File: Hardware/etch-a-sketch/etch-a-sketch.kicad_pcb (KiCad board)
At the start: 2 copper layers, 100 x 42 mm, 37 parts, among them J1 USART, J2 Conn_02x05_Odd_Even, J3 OLED, J4 Power Connector, SW1 Encoder 1, SW2 Encoder 2, U1 AMS1117-3.3, U2 STM32F401RET6

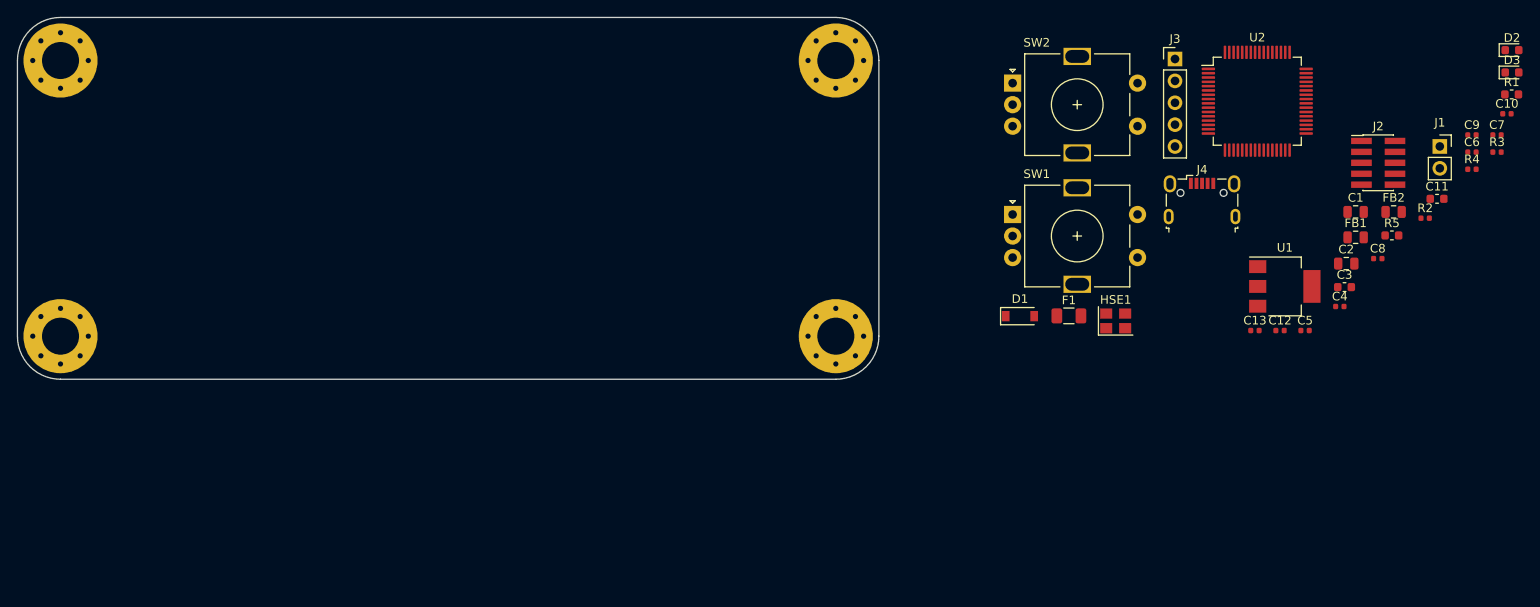
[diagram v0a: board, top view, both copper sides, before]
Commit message: fix: resize PCB outline to be 62mm tall
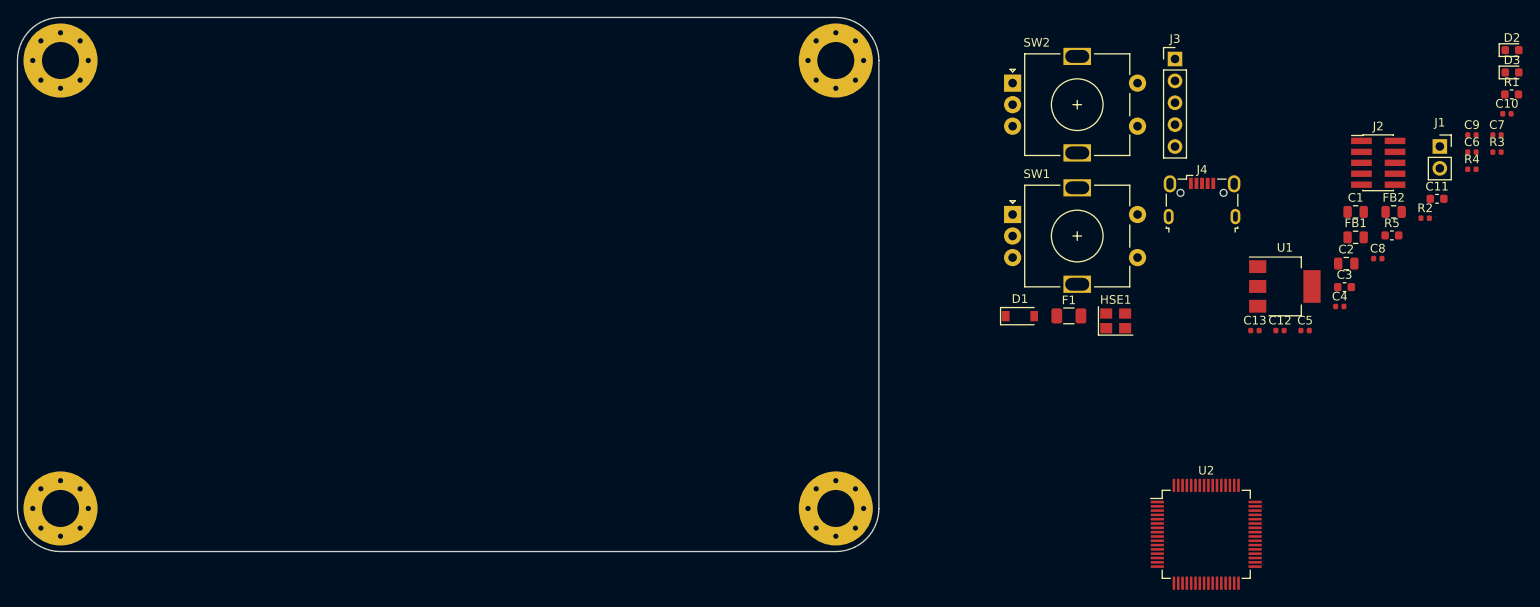
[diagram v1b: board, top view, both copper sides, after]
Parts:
- moved U2 50.6 mm to (158.0, 80.0)
- moved H3 20.0 mm to (25.0, 77.0)
- moved H4 20.0 mm to (115.0, 77.0)
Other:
- board size 100 x 42 mm -> 100 x 62 mm
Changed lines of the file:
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@@
   )
   (module MountingHole:MountingHole_4.3mm_M4_Pad_Via (layer F.Cu)
-    (at 25 57)
+    (at 25 77)
     (descr "Mounting Hole 4.3mm, M4")
     (tags "mounting hole 4.3mm m4")
@@
   )
   (module MountingHole:MountingHole_4.3mm_M4_Pad_Via (layer F.Cu)
-    (at 115 57)
+    (at 115 77)
     (descr "Mounting Hole 4.3mm, M4")
     (tags "mounting hole 4.3mm m4")
@@
   )
   (module Package_QFP:LQFP-64_10x10mm_P0.5mm (layer F.Cu)
-    (at 163.925001 29.725001)
+    (at 158 80)
     (descr "LQFP, 64 Pin (https://www.analog.com/media/en/technical-documentation/data-sheets/ad7606_7606-6_7606-4.pdf), generated with kicad-footprint-generator ipc_gullwing_generator.py")
     (tags "LQFP QFP")
@@
     )
   )
-  (gr_arc (start 115 57) (end 115 62) (angle -90) (layer Edge.Cuts) (width 0.05))
+  (gr_arc (start 115 77) (end 115 82) (angle -90) (layer Edge.Cuts) (width 0.05))
   (gr_arc (start 115 25) (end 120 25) (angle -90) (layer Edge.Cuts) (width 0.05))
-  (gr_arc (start 25 57) (end 20 57) (angle -90) (layer Edge.Cuts) (width 0.05))
+  (gr_arc (start 25 77) (end 20 77) (angle -90) (layer Edge.Cuts) (width 0.05))
   (gr_line (start 25 20) (end 115 20) (layer Edge.Cuts) (width 0.05))
   (gr_arc (start 25 25) (end 25 20) (angle -90) (layer Edge.Cuts) (width 0.05))
-  (gr_line (start 20 57) (end 20 25) (layer Edge.Cuts) (width 0.05))
-  (gr_line (start 115 62) (end 25 62) (layer Edge.Cuts) (width 0.05))
-  (gr_line (start 120 25) (end 120 57) (layer Edge.Cuts) (width 0.05))
+  (gr_line (start 20 77) (end 20 25) (layer Edge.Cuts) (width 0.05))
+  (gr_line (start 115 82) (end 25 82) (layer Edge.Cuts) (width 0.05))
+  (gr_line (start 120 25) (end 120 77) (layer Edge.Cuts) (width 0.05))
 )

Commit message: feat: move MCU to centre of board
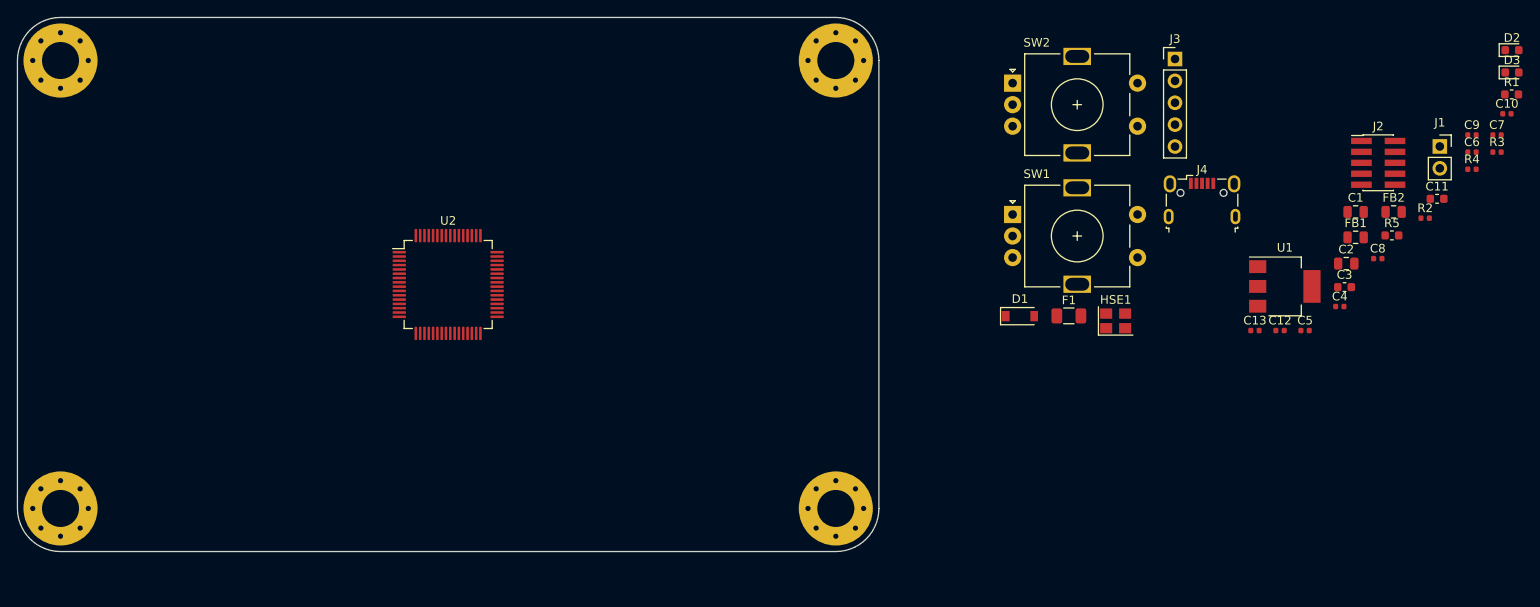
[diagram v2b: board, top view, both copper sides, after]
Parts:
- moved U2 92.7 mm to (70.0, 51.0)
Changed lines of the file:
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@@
   )
   (module Package_QFP:LQFP-64_10x10mm_P0.5mm (layer F.Cu)
-    (at 158 80)
+    (at 70 51)
     (descr "LQFP, 64 Pin (https://www.analog.com/media/en/technical-documentation/data-sheets/ad7606_7606-6_7606-4.pdf), generated with kicad-footprint-generator ipc_gullwing_generator.py")
     (tags "LQFP QFP")

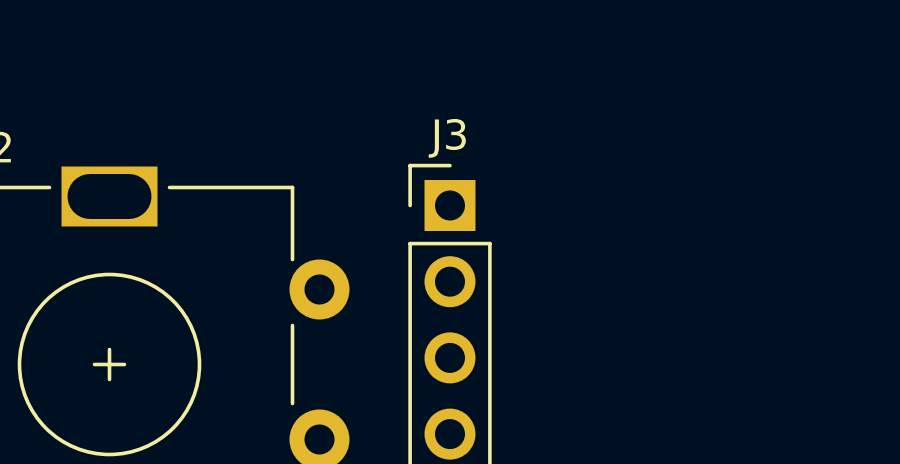
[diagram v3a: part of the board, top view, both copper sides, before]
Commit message: fix: actually maybe better to keep the OLED socketed
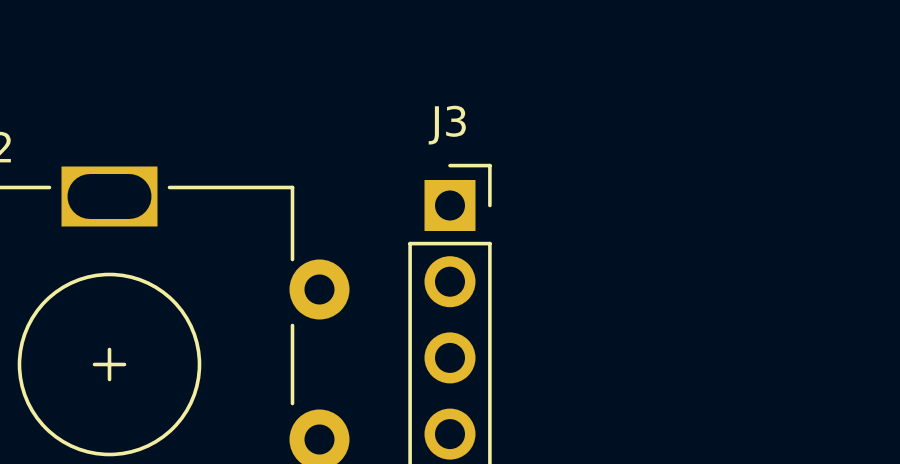
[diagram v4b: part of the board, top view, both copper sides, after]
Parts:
- J3: footprint Connector_PinHeader_2.54mm:PinHeader_1x05_P2.54mm_Vertical -> Connector_PinSocket_2.54mm:PinSocket_1x05_P2.54mm_Vertical
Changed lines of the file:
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@@
     (add_net VCC)
+  )
+  (module Connector_PinSocket_2.54mm:PinSocket_1x05_P2.54mm_Vertical (layer F.Cu)
+    (at 154.375001 24.825001)
+    (descr "Through hole straight socket strip, 1x05, 2.54mm pitch, single row (from Kicad 4.0.7), script generated")
+    (tags "Through hole socket strip THT 1x05 2.54mm single row")
+    (fp_text reference J3 (at 0 -2.77) (layer F.SilkS)
+      (effects (font (size 1 1) (thickness 0.15)))
+    )
+    (fp_text value OLED (at 0 12.93) (layer F.Fab)
+      (effects (font (size 1 1) (thickness 0.15)))
+    )
+    (fp_text user %R (at 0 5.08 90) (layer F.Fab)
+      (effects (font (size 1 1) (thickness 0.15)))
+    )
+    (fp_line (start -1.8 11.9) (end -1.8 -1.8) (layer F.CrtYd) (width 0.05))
+    (fp_line (start 1.75 11.9) (end -1.8 11.9) (layer F.CrtYd) (width 0.05))
+    (fp_line (start 1.75 -1.8) (end 1.75 11.9) (layer F.CrtYd) (width 0.05))
+    (fp_line (start -1.8 -1.8) (end 1.75 -1.8) (layer F.CrtYd) (width 0.05))
+    (fp_line (start 0 -1.33) (end 1.33 -1.33) (layer F.SilkS) (width 0.12))
+    (fp_line (start 1.33 -1.33) (end 1.33 0) (layer F.SilkS) (width 0.12))
+    (fp_line (start 1.33 1.27) (end 1.33 11.49) (layer F.SilkS) (width 0.12))
+    (fp_line (start -1.33 11.49) (end 1.33 11.49) (layer F.SilkS) (width 0.12))
+    (fp_line (start -1.33 1.27) (end -1.33 11.49) (layer F.SilkS) (width 0.12))
+    (fp_line (start -1.33 1.27) (end 1.33 1.27) (layer F.SilkS) (width 0.12))
+    (fp_line (start -1.27 11.43) (end -1.27 -1.27) (layer F.Fab) (width 0.1))
+    (fp_line (start 1.27 11.43) (end -1.27 11.43) (layer F.Fab) (width 0.1))
+    (fp_line (start 1.27 -0.635) (end 1.27 11.43) (layer F.Fab) (width 0.1))
+    (fp_line (start 0.635 -1.27) (end 1.27 -0.635) (layer F.Fab) (width 0.1))
+    (fp_line (start -1.27 -1.27) (end 0.635 -1.27) (layer F.Fab) (width 0.1))
+    (pad 5 thru_hole oval (at 0 10.16) (size 1.7 1.7) (drill 1) (layers *.Cu *.Mask)
+      (net 1 GND))
+    (pad 4 thru_hole oval (at 0 7.62) (size 1.7 1.7) (drill 1) (layers *.Cu *.Mask)
+      (net 24 "Net-(J3-Pad4)"))
+    (pad 3 thru_hole oval (at 0 5.08) (size 1.7 1.7) (drill 1) (layers *.Cu *.Mask)
+      (net 23 OLED_SCL))
+    (pad 2 thru_hole oval (at 0 2.54) (size 1.7 1.7) (drill 1) (layers *.Cu *.Mask)
+      (net 22 OLED_SDA))
+    (pad 1 thru_hole rect (at 0 0) (size 1.7 1.7) (drill 1) (layers *.Cu *.Mask)
+      (net 3 +3V3))
+    (model ${KISYS3DMOD}/Connector_PinSocket_2.54mm.3dshapes/PinSocket_1x05_P2.54mm_Vertical.wrl
+      (at (xyz 0 0 0))
+      (scale (xyz 1 1 1))
+      (rotate (xyz 0 0 0))
+    )
   )
   (module Capacitor_SMD:C_0805_2012Metric (layer F.Cu)
@@
       (at (xyz 0 0 0))
       (scale (xyz 1 1 1))
-      (rotate (xyz 0 0 0))
-    )
-  )
-  (module Connector_PinHeader_2.54mm:PinHeader_1x05_P2.54mm_Vertical (layer F.Cu)
-    (at 154.375001 24.825001)
-    (descr "Through hole straight pin header, 1x05, 2.54mm pitch, single row")
-    (tags "Through hole pin header THT 1x05 2.54mm single row")
-    (fp_text reference J3 (at 0 -2.33) (layer F.SilkS)
-      (effects (font (size 1 1) (thickness 0.15)))
-    )
-    (fp_text value OLED (at 0 12.49) (layer F.Fab)
-      (effects (font (size 1 1) (thickness 0.15)))
-    )
-    (fp_line (start -0.635 -1.27) (end 1.27 -1.27) (layer F.Fab) (width 0.1))
-    (fp_line (start 1.27 -1.27) (end 1.27 11.43) (layer F.Fab) (width 0.1))
-    (fp_line (start 1.27 11.43) (end -1.27 11.43) (layer F.Fab) (width 0.1))
-    (fp_line (start -1.27 11.43) (end -1.27 -0.635) (layer F.Fab) (width 0.1))
-    (fp_line (start -1.27 -0.635) (end -0.635 -1.27) (layer F.Fab) (width 0.1))
-    (fp_line (start -1.33 11.49) (end 1.33 11.49) (layer F.SilkS) (width 0.12))
-    (fp_line (start -1.33 1.27) (end -1.33 11.49) (layer F.SilkS) (width 0.12))
-    (fp_line (start 1.33 1.27) (end 1.33 11.49) (layer F.SilkS) (width 0.12))
-    (fp_line (start -1.33 1.27) (end 1.33 1.27) (layer F.SilkS) (width 0.12))
-    (fp_line (start -1.33 0) (end -1.33 -1.33) (layer F.SilkS) (width 0.12))
-    (fp_line (start -1.33 -1.33) (end 0 -1.33) (layer F.SilkS) (width 0.12))
-    (fp_line (start -1.8 -1.8) (end -1.8 11.95) (layer F.CrtYd) (width 0.05))
-    (fp_line (start -1.8 11.95) (end 1.8 11.95) (layer F.CrtYd) (width 0.05))
-    (fp_line (start 1.8 11.95) (end 1.8 -1.8) (layer F.CrtYd) (width 0.05))
-    (fp_line (start 1.8 -1.8) (end -1.8 -1.8) (layer F.CrtYd) (width 0.05))
-    (fp_text user %R (at 0 5.08 90) (layer F.Fab)
-      (effects (font (size 1 1) (thickness 0.15)))
-    )
-    (pad 1 thru_hole rect (at 0 0) (size 1.7 1.7) (drill 1) (layers *.Cu *.Mask)
-      (net 3 +3V3))
-    (pad 2 thru_hole oval (at 0 2.54) (size 1.7 1.7) (drill 1) (layers *.Cu *.Mask)
-      (net 22 OLED_SDA))
-    (pad 3 thru_hole oval (at 0 5.08) (size 1.7 1.7) (drill 1) (layers *.Cu *.Mask)
-      (net 23 OLED_SCL))
-    (pad 4 thru_hole oval (at 0 7.62) (size 1.7 1.7) (drill 1) (layers *.Cu *.Mask)
-      (net 24 "Net-(J3-Pad4)"))
-    (pad 5 thru_hole oval (at 0 10.16) (size 1.7 1.7) (drill 1) (layers *.Cu *.Mask)
-      (net 1 GND))
-    (model ${KISYS3DMOD}/Connector_PinHeader_2.54mm.3dshapes/PinHeader_1x05_P2.54mm_Vertical.wrl
-      (at (xyz 0 0 0))
-      (scale (xyz 1 1 1))

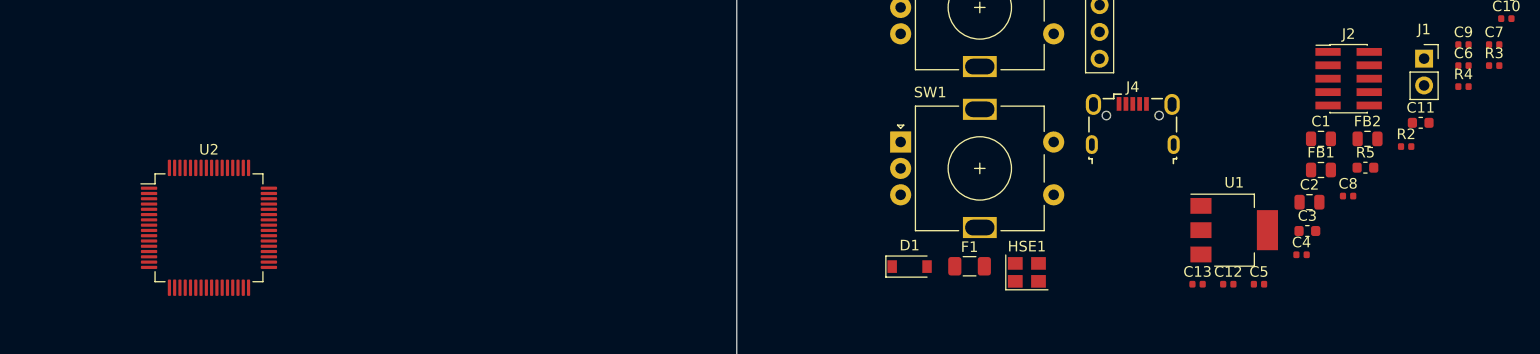
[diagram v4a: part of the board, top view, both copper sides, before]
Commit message: feat: place HSE
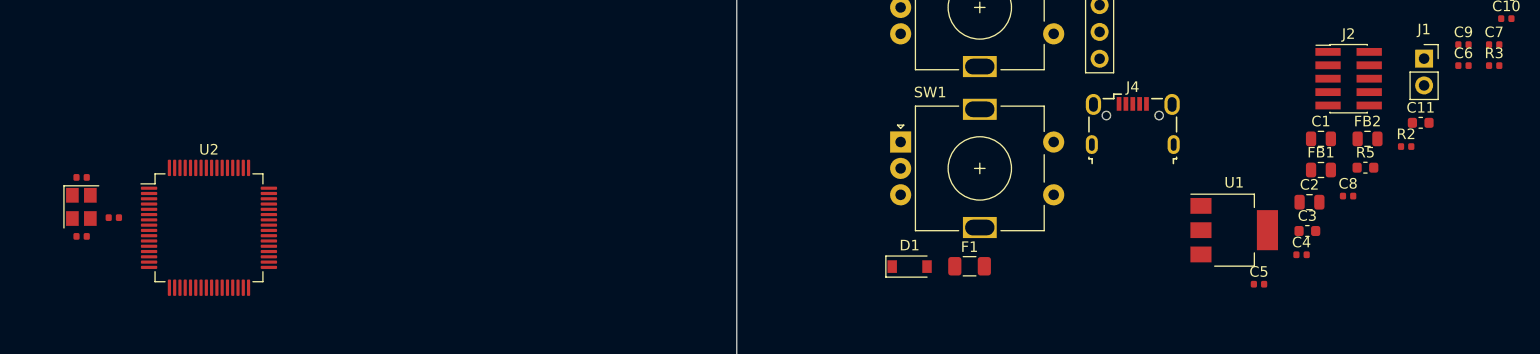
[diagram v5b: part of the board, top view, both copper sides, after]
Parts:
- moved R4 128.5 mm to (61.0, 50.0), turned to 180 degrees
- moved C12 109.1 mm to (57.9, 46.2)
- moved C13 105.8 mm to (57.9, 51.8), turned to 180 degrees
- moved HSE1 89.8 mm to (57.9, 49.0), turned to 270 degrees
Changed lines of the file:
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@@
   )
   (module Capacitor_SMD:C_0402_1005Metric (layer F.Cu)
-    (at 166.565001 56.345001)
+    (at 57.935 46.228)
     (descr "Capacitor SMD 0402 (1005 Metric), square (rectangular) end terminal, IPC_7351 nominal, (Body size source: http://www.tortai-tech.com/upload/download/2011102023233369053.pdf), generated with kicad-footprint-generator")
     (tags capacitor)
     (attr smd)
-    (fp_text reference C12 (at 0 -1.17) (layer F.SilkS)
+    (fp_text reference C12 (at 0 -1.17) (layer F.Fab)
       (effects (font (size 1 1) (thickness 0.15)))
     )
@@
   )
   (module Capacitor_SMD:C_0402_1005Metric (layer F.Cu)
-    (at 163.655001 56.345001)
+    (at 57.935 51.816 180)
     (descr "Capacitor SMD 0402 (1005 Metric), square (rectangular) end terminal, IPC_7351 nominal, (Body size source: http://www.tortai-tech.com/upload/download/2011102023233369053.pdf), generated with kicad-footprint-generator")
     (tags capacitor)
     (attr smd)
-    (fp_text reference C13 (at 0 -1.17) (layer F.SilkS)
+    (fp_text reference C13 (at 0 1.27) (layer F.Fab)
       (effects (font (size 1 1) (thickness 0.15)))
     )
@@
     (fp_line (start -0.5 -0.25) (end 0.5 -0.25) (layer F.Fab) (width 0.1))
     (fp_line (start -0.5 0.25) (end -0.5 -0.25) (layer F.Fab) (width 0.1))
-    (pad 2 smd roundrect (at 0.485 0) (size 0.59 0.64) (layers F.Cu F.Paste F.Mask) (roundrect_rratio 0.25)
-      (net 1 GND))
-    (pad 1 smd roundrect (at -0.485 0) (size 0.59 0.64) (layers F.Cu F.Paste F.Mask) (roundrect_rratio 0.25)
+    (pad 2 smd roundrect (at 0.485 0 180) (size 0.59 0.64) (layers F.Cu F.Paste F.Mask) (roundrect_rratio 0.25)
+      (net 1 GND))
+    (pad 1 smd roundrect (at -0.485 0 180) (size 0.59 0.64) (layers F.Cu F.Paste F.Mask) (roundrect_rratio 0.25)
       (net 7 "Net-(C13-Pad1)"))
     (model ${KISYS3DMOD}/Capacitor_SMD.3dshapes/C_0402_1005Metric.wrl
@@
   )
   (module Crystal:Crystal_SMD_3225-4Pin_3.2x2.5mm (layer F.Cu)
-    (at 147.485001 55.225001)
+    (at 57.912 49.022 270)
     (descr "SMD Crystal SERIES SMD3225/4 http://www.txccrystal.com/images/pdf/7m-accuracy.pdf, 3.2x2.5mm^2 package")
     (tags "SMD SMT crystal")
     (attr smd)
-    (fp_text reference HSE1 (at 0 -2.45) (layer F.SilkS)
-      (effects (font (size 1 1) (thickness 0.15)))
-    )
-    (fp_text value 16MHz (at 0 2.45) (layer F.Fab)
-      (effects (font (size 1 1) (thickness 0.15)))
-    )
-    (fp_text user %R (at 0 0) (layer F.Fab)
+    (fp_text reference HSE1 (at 0 -2.45 90) (layer F.Fab)
+      (effects (font (size 1 1) (thickness 0.15)))
+    )
+    (fp_text value 16MHz (at 0 2.45 90) (layer F.Fab)
+      (effects (font (size 1 1) (thickness 0.15)))
+    )
+    (fp_text user %R (at 0 0 90) (layer F.Fab)
       (effects (font (size 0.7 0.7) (thickness 0.105)))
     )
@@
     (fp_line (start 2.1 1.7) (end 2.1 -1.7) (layer F.CrtYd) (width 0.05))
     (fp_line (start 2.1 -1.7) (end -2.1 -1.7) (layer F.CrtYd) (width 0.05))
-    (pad 1 smd rect (at -1.1 0.85) (size 1.4 1.2) (layers F.Cu F.Paste F.Mask)
+    (pad 1 smd rect (at -1.1 0.85 270) (size 1.4 1.2) (layers F.Cu F.Paste F.Mask)
       (net 6 HSE_IN))
-    (pad 2 smd rect (at 1.1 0.85) (size 1.4 1.2) (layers F.Cu F.Paste F.Mask)
-      (net 1 GND))
-    (pad 3 smd rect (at 1.1 -0.85) (size 1.4 1.2) (layers F.Cu F.Paste F.Mask)
+    (pad 2 smd rect (at 1.1 0.85 270) (size 1.4 1.2) (layers F.Cu F.Paste F.Mask)
+      (net 1 GND))
+    (pad 3 smd rect (at 1.1 -0.85 270) (size 1.4 1.2) (layers F.Cu F.Paste F.Mask)
       (net 7 "Net-(C13-Pad1)"))
-    (pad 4 smd rect (at -1.1 -0.85) (size 1.4 1.2) (layers F.Cu F.Paste F.Mask)
+    (pad 4 smd rect (at -1.1 -0.85 270) (size 1.4 1.2) (layers F.Cu F.Paste F.Mask)
       (net 1 GND))
     (model ${KISYS3DMOD}/Crystal.3dshapes/Crystal_SMD_3225-4Pin_3.2x2.5mm.wrl
@@
   )
   (module Resistor_SMD:R_0402_1005Metric (layer F.Cu)
-    (at 188.845001 37.625001)
+    (at 60.985 50.038 180)
     (descr "Resistor SMD 0402 (1005 Metric), square (rectangular) end terminal, IPC_7351 nominal, (Body size source: http://www.tortai-tech.com/upload/download/2011102023233369053.pdf), generated with kicad-footprint-generator")
     (tags resistor)
     (attr smd)
-    (fp_text reference R4 (at 0 -1.17) (layer F.SilkS)
+    (fp_text reference R4 (at -3.579 -4.064) (layer F.Fab)
       (effects (font (size 1 1) (thickness 0.15)))
     )
@@
       (effects (font (size 0.25 0.25) (thickness 0.04)))
     )
-    (pad 1 smd roundrect (at -0.485 0) (size 0.59 0.64) (layers F.Cu F.Paste F.Mask) (roundrect_rratio 0.25)
+    (pad 1 smd roundrect (at -0.485 0 180) (size 0.59 0.64) (layers F.Cu F.Paste F.Mask) (roundrect_rratio 0.25)
       (net 29 HSE_OUT))
-    (pad 2 smd roundrect (at 0.485 0) (size 0.59 0.64) (layers F.Cu F.Paste F.Mask) (roundrect_rratio 0.25)
+    (pad 2 smd roundrect (at 0.485 0 180) (size 0.59 0.64) (layers F.Cu F.Paste F.Mask) (roundrect_rratio 0.25)
       (net 7 "Net-(C13-Pad1)"))
     (model ${KISYS3DMOD}/Resistor_SMD.3dshapes/R_0402_1005Metric.wrl
